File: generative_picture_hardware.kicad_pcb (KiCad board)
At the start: 2 copper layers, 100 x 100 mm, 63 parts, among them J1 e_Paper_HAT, J2 Conn_ARM_JTAG_SWD_10, J3 USB_C_Receptacle_USB2.0, Q1 PMN48XP, Q2 DMG9926UDM, Q3 MBT3904DW1, SW1 SW_Push, SW2 SW_Push, U1 AP2112K-3.3, U2 ESP32-WROOM-32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

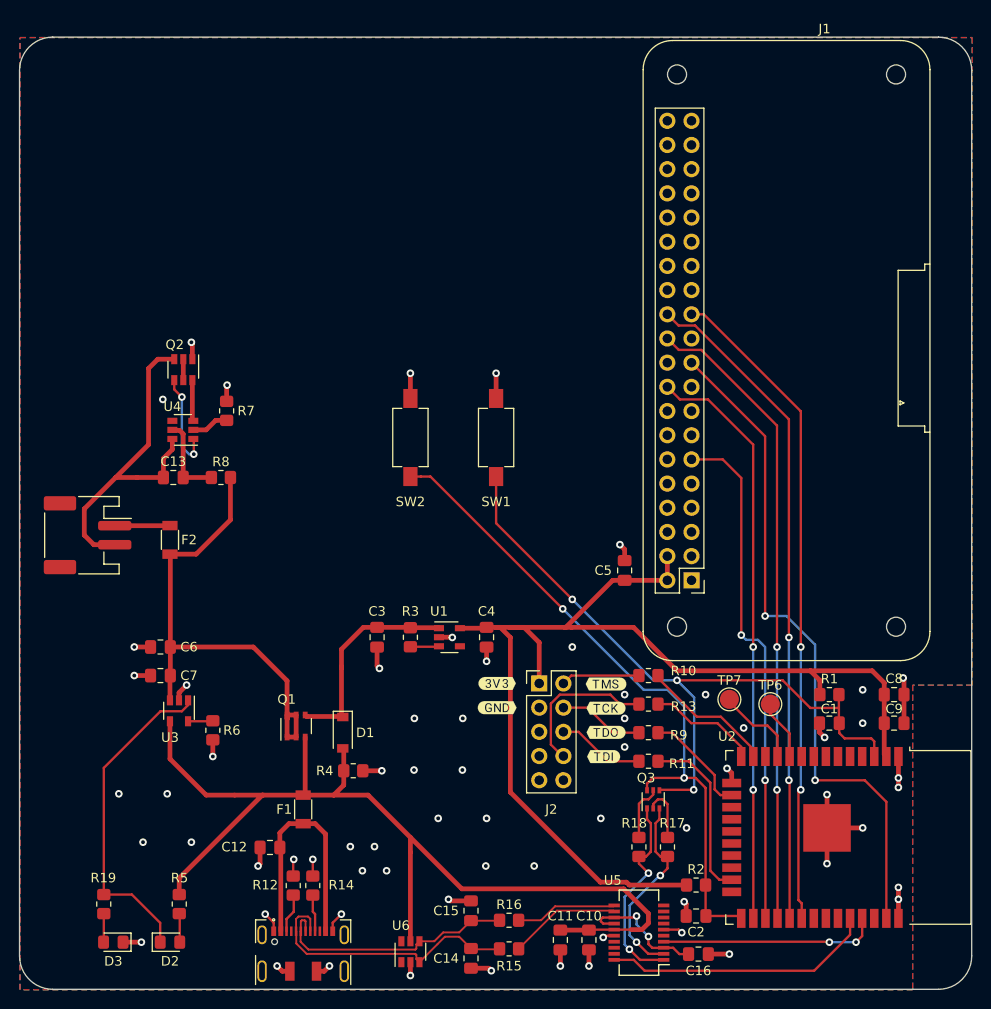
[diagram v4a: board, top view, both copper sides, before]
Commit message: Adds some more labels
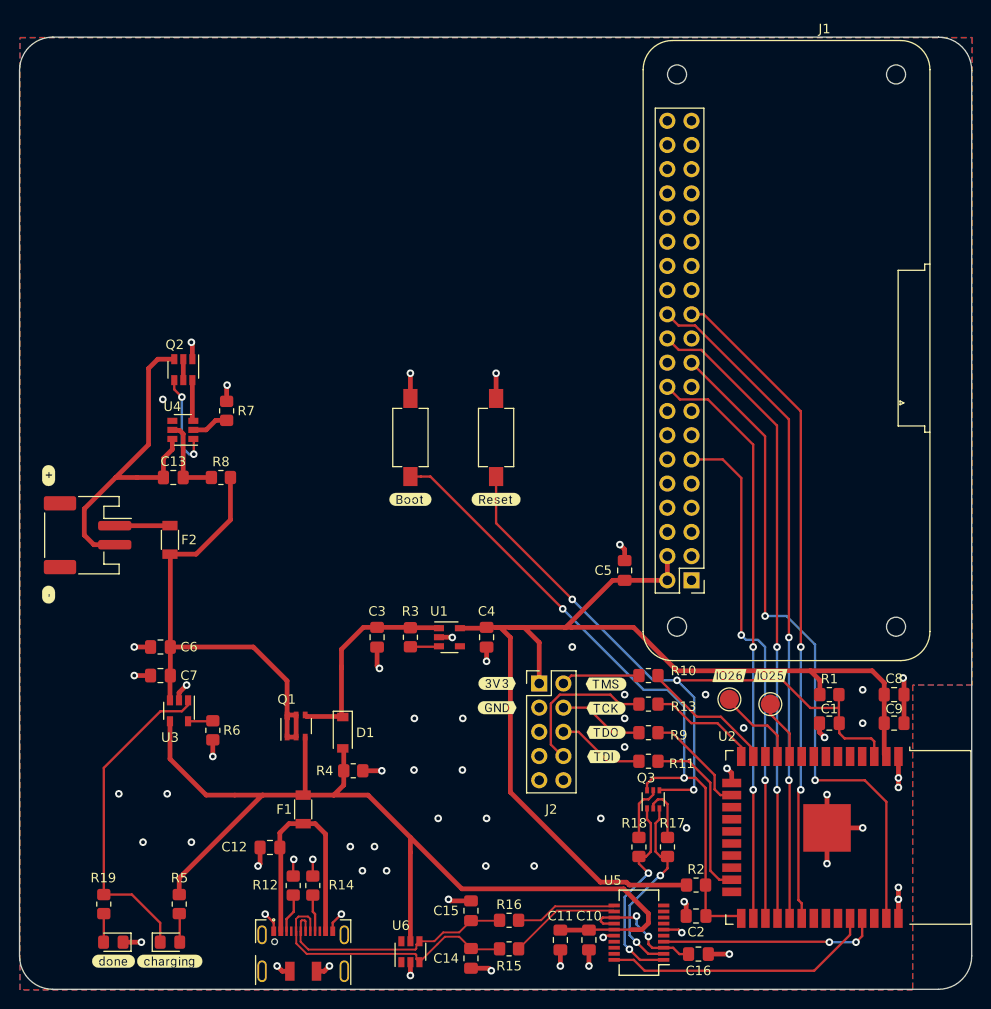
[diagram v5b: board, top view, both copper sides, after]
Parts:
- added ?: , buzzardLabel, F.Cu at (103.0, 110.5)
- added ?: , buzzardLabel, F.Cu at (141.0, 100.5)
- added ?: , buzzardLabel, F.Cu at (178.8, 119.0)
- added ?: , buzzardLabel, F.Cu at (103.0, 98.0)
- added ?: , buzzardLabel, F.Cu at (150.0, 100.5)
- added ?: , buzzardLabel, F.Cu at (115.7, 149.0)
- added ?: , buzzardLabel, F.Cu at (109.8, 149.0)
- added ?: , buzzardLabel, F.Cu at (174.5, 119.0)

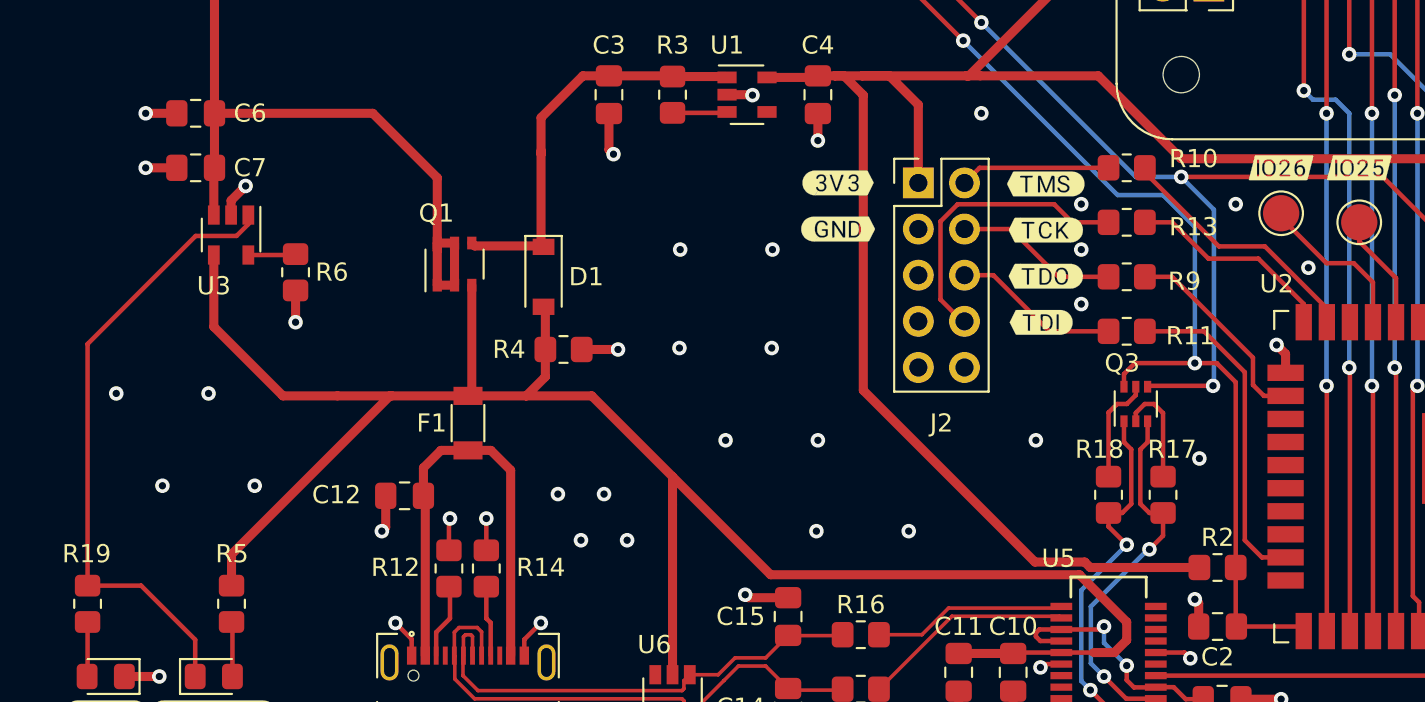
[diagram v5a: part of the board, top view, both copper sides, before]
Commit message: Cleans up the extra vias
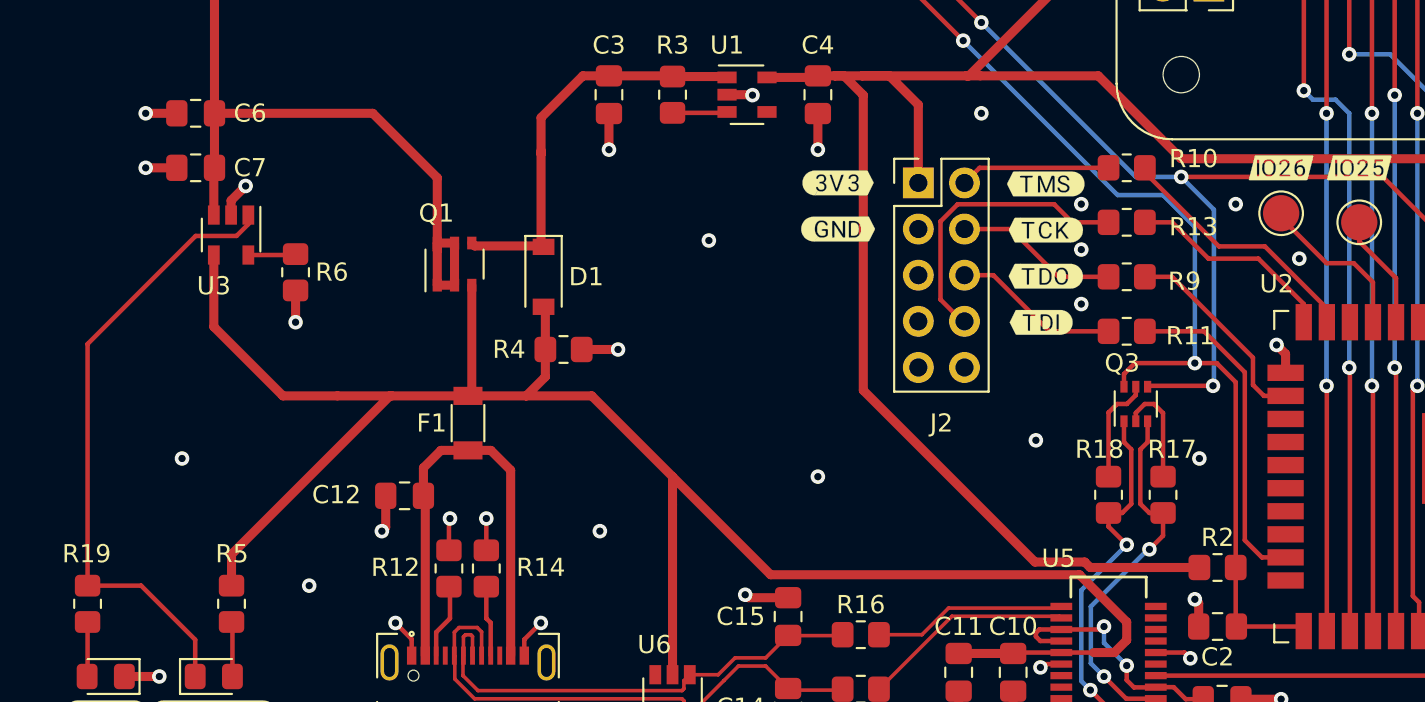
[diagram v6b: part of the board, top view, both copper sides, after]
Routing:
- net GND: track 82.3 -> 82.5 mm, vias 67 -> 56
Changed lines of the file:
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@@
   (segment (start 147.3625 149.7375) (end 149.2375 149.7375) (width 0.5) (layer "F.Cu") (net 3))
   (segment (start 169.9625 144.25) (end 169.9625 142.9625) (width 0.5) (layer "F.Cu") (net 3))
-  (segment (start 137.5 116.0125) (end 137.5 118) (width 0.5) (layer "F.Cu") (net 3))
   (segment (start 118.1 85.775) (end 118.1 84.1) (width 0.5) (layer "F.Cu") (net 3))
   (segment (start 147.3625 142.6625) (end 145.1625 142.6625) (width 0.5) (layer "F.Cu") (net 3))
@@
   (segment (start 136 129) (end 138 129) (width 0.5) (layer "F.Cu") (net 3))
   (segment (start 141 149.102479) (end 141 150.5) (width 0.5) (layer "F.Cu") (net 3))
-  (segment (start 137.5 118) (end 137.75 118.25) (width 0.5) (layer "F.Cu") (net 3))
+  (segment (start 149 116.0125) (end 149 118) (width 0.5) (layer "F.Cu") (net 3))
   (segment (start 192.75 119.25) (end 192.8375 119.3375) (width 0.5) (layer "F.Cu") (net 3))
   (segment (start 116.7 120.8) (end 117.5 120) (width 0.5) (layer "F.Cu") (net 3))
@@
   (segment (start 120.25 125.75) (end 120.25 127.5) (width 0.5) (layer "F.Cu") (net 3))
   (segment (start 161.4325 146.3175) (end 161.25 146.5) (width 0.25) (layer "F.Cu") (net 3))
+  (segment (start 137.5 118) (end 137.5 116.0125) (width 0.5) (layer "F.Cu") (net 3))
   (segment (start 128.6925 140.054098) (end 128.6925 138.361598) (width 0.25) (layer "F.Cu") (net 3))
   (segment (start 163.5 105.75) (end 163 105.25) (width 0.5) (layer "F.Cu") (net 3))
-  (segment (start 149 116.0125) (end 149 117.5) (width 0.5) (layer "F.Cu") (net 3))
   (segment (start 192.8375 119.3375) (end 192.8375 121) (width 0.5) (layer "F.Cu") (net 3))
   (segment (start 184.755 134.999748) (end 184.755 131.505) (width 0.5) (layer "F.Cu") (net 3))
@@
   (via (at 117.5 120) (size 0.8) (drill 0.4) (layers "F.Cu" "B.Cu") (net 3))
   (via (at 184.5 125.5) (size 0.8) (drill 0.4) (layers "F.Cu" "B.Cu") (net 3))
-  (via (at 146.46 128.92) (size 0.8) (drill 0.4) (layers "F.Cu" "B.Cu") (free) (net 3))
   (via (at 118 84) (size 0.8) (drill 0.4) (layers "F.Cu" "B.Cu") (net 3))
   (via (at 156.75 149.5) (size 0.8) (drill 0.4) (layers "F.Cu" "B.Cu") (net 3))
@@
   (via (at 120.25 127.5) (size 0.8) (drill 0.4) (layers "F.Cu" "B.Cu") (net 3))
   (via (at 163.5 126.5) (size 0.8) (drill 0.4) (layers "F.Cu" "B.Cu") (free) (net 3))
-  (via (at 137.23 136.96) (size 0.8) (drill 0.4) (layers "F.Cu" "B.Cu") (free) (net 3))
-  (via (at 176 124.5) (size 0.8) (drill 0.4) (layers "F.Cu" "B.Cu") (free) (net 3))
   (via (at 145.4 115) (size 0.8) (drill 0.4) (layers "F.Cu" "B.Cu") (net 3))
+  (via (at 137.5 118) (size 0.8) (drill 0.4) (layers "F.Cu" "B.Cu") (net 3))
   (via (at 130.75 138.304098) (size 0.8) (drill 0.4) (layers "F.Cu" "B.Cu") (net 3))
-  (via (at 110.38 131.42) (size 0.8) (drill 0.4) (layers "F.Cu" "B.Cu") (free) (net 3))
   (via (at 161 134) (size 0.8) (drill 0.4) (layers "F.Cu" "B.Cu") (free) (net 3))
   (via (at 128.75 138.304098) (size 0.8) (drill 0.4) (layers "F.Cu" "B.Cu") (net 3))
-  (via (at 143.92 134) (size 0.8) (drill 0.4) (layers "F.Cu" "B.Cu") (free) (net 3))
-  (via (at 148.92 139) (size 0.8) (drill 0.4) (layers "F.Cu" "B.Cu") (free) (net 3))
   (via (at 132.5 149.5) (size 0.8) (drill 0.4) (layers "F.Cu" "B.Cu") (net 3))
   (via (at 127 149.5) (size 0.8) (drill 0.4) (layers "F.Cu" "B.Cu") (net 3))
-  (via (at 112.92 136.5) (size 0.8) (drill 0.4) (layers "F.Cu" "B.Cu") (free) (net 3))
   (via (at 163.5 123.5) (size 0.8) (drill 0.4) (layers "F.Cu" "B.Cu") (free) (net 3))
   (via (at 133.75 144.054098) (size 0.8) (drill 0.4) (layers "F.Cu" "B.Cu") (net 3))
   (via (at 150 87.25) (size 0.8) (drill 0.4) (layers "F.Cu" "B.Cu") (net 3))
-  (via (at 149 134) (size 0.8) (drill 0.4) (layers "F.Cu" "B.Cu") (free) (net 3))
-  (via (at 149 117.5) (size 0.8) (drill 0.4) (layers "F.Cu" "B.Cu") (net 3))
-  (via (at 141.38 128.92) (size 0.8) (drill 0.4) (layers "F.Cu" "B.Cu") (free) (net 3))
-  (via (at 115.46 131.42) (size 0.8) (drill 0.4) (layers "F.Cu" "B.Cu") (free) (net 3))
-  (via (at 134.69 136.96) (size 0.8) (drill 0.4) (layers "F.Cu" "B.Cu") (free) (net 3))
   (via (at 192.75 119.25) (size 0.8) (drill 0.4) (layers "F.Cu" "B.Cu") (net 3))
   (via (at 141 87.25) (size 0.8) (drill 0.4) (layers "F.Cu" "B.Cu") (net 3))
   (via (at 121.75 88.5) (size 0.8) (drill 0.4) (layers "F.Cu" "B.Cu") (net 3))
+  (via (at 149 136) (size 0.8) (drill 0.4) (layers "F.Cu" "B.Cu") (free) (net 3))
   (via (at 184.75 131.5) (size 0.8) (drill 0.4) (layers "F.Cu" "B.Cu") (net 3))
-  (via (at 137.75 118.25) (size 0.8) (drill 0.4) (layers "F.Cu" "B.Cu") (net 3))
+  (via (at 149 118) (size 0.8) (drill 0.4) (layers "F.Cu" "B.Cu") (net 3))
+  (via (at 175.5 124) (size 0.8) (drill 0.4) (layers "F.Cu" "B.Cu") (free) (net 3))
   (via (at 141 150.5) (size 0.8) (drill 0.4) (layers "F.Cu" "B.Cu") (net 3))
   (via (at 158 116) (size 0.8) (drill 0.4) (layers "F.Cu" "B.Cu") (free) (net 3))
   (via (at 192.25 130.75) (size 0.8) (drill 0.4) (layers "F.Cu" "B.Cu") (net 3))
   (via (at 170 135) (size 0.8) (drill 0.4) (layers "F.Cu" "B.Cu") (free) (net 3))
-  (via (at 118 136.5) (size 0.8) (drill 0.4) (layers "F.Cu" "B.Cu") (free) (net 3))
   (via (at 149.5 150) (size 0.8) (drill 0.4) (layers "F.Cu" "B.Cu") (net 3))
   (via (at 172 121) (size 0.8) (drill 0.4) (layers "F.Cu" "B.Cu") (free) (net 3))
   (via (at 159.75 149.5) (size 0.8) (drill 0.4) (layers "F.Cu" "B.Cu") (net 3))
   (via (at 112.75 147) (size 0.8) (drill 0.4) (layers "F.Cu" "B.Cu") (net 3))
-  (via (at 135.96 139.5) (size 0.8) (drill 0.4) (layers "F.Cu" "B.Cu") (free) (net 3))
-  (via (at 146.5 123.5) (size 0.8) (drill 0.4) (layers "F.Cu" "B.Cu") (free) (net 3))
   (via (at 138 129) (size 0.8) (drill 0.4) (layers "F.Cu" "B.Cu") (net 3))
+  (via (at 114 135) (size 0.8) (drill 0.4) (layers "F.Cu" "B.Cu") (free) (net 3))
   (via (at 145 142.5) (size 0.8) (drill 0.4) (layers "F.Cu" "B.Cu") (net 3))
   (via (at 169.5 146) (size 0.8) (drill 0.4) (layers "F.Cu" "B.Cu") (net 3))
@@
   (via (at 192.25 142.5) (size 0.8) (drill 0.4) (layers "F.Cu" "B.Cu") (net 3))
   (via (at 125 139) (size 0.8) (drill 0.4) (layers "F.Cu" "B.Cu") (net 3))
-  (via (at 138.5 139.5) (size 0.8) (drill 0.4) (layers "F.Cu" "B.Cu") (free) (net 3))
+  (via (at 137 139) (size 0.8) (drill 0.4) (layers "F.Cu" "B.Cu") (free) (net 3))
+  (via (at 143 123) (size 0.8) (drill 0.4) (layers "F.Cu" "B.Cu") (free) (net 3))
   (via (at 174.25 128.75) (size 0.8) (drill 0.4) (layers "F.Cu" "B.Cu") (net 3))
-  (via (at 141.42 123.5) (size 0.8) (drill 0.4) (layers "F.Cu" "B.Cu") (free) (net 3))
+  (via (at 121 142) (size 0.8) (drill 0.4) (layers "F.Cu" "B.Cu") (free) (net 3))
   (via (at 192.25 141.25) (size 0.8) (drill 0.4) (layers "F.Cu" "B.Cu") (net 3))
   (via (at 188.5 135) (size 0.8) (drill 0.4) (layers "F.Cu" "B.Cu") (net 3))
@@
   (via (at 161.25 146.5) (size 0.8) (drill 0.4) (layers "F.Cu" "B.Cu") (net 3))
   (via (at 174.5 148.25) (size 0.8) (drill 0.4) (layers "F.Cu" "B.Cu") (net 3))
-  (via (at 154 139) (size 0.8) (drill 0.4) (layers "F.Cu" "B.Cu") (free) (net 3))
   (segment (start 186 122.4) (end 186 123.9625) (width 0.25) (layer "F.Cu") (net 4))
   (segment (start 167.2 131) (end 167.15 131.05) (width 0.25) (layer "F.Cu") (net 4))

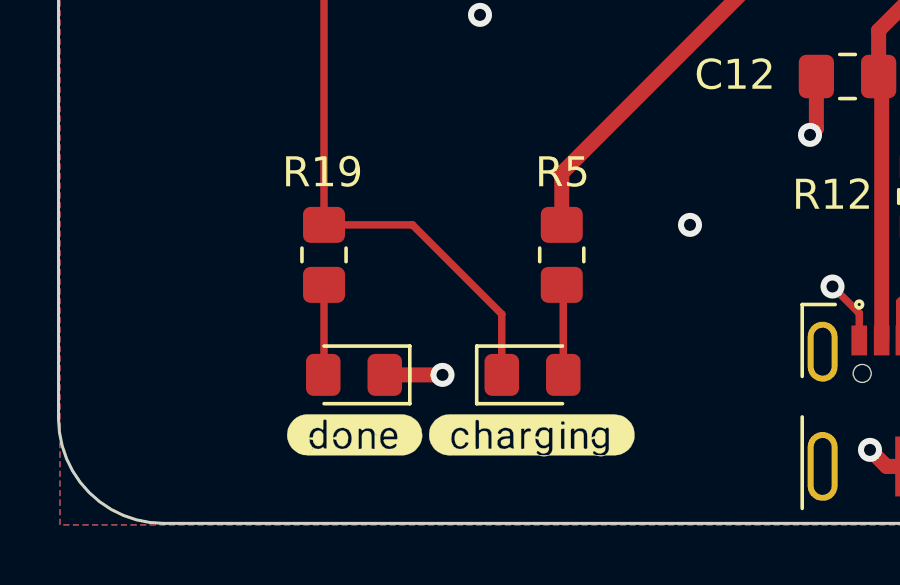
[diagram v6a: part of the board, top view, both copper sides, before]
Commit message: Adds logo
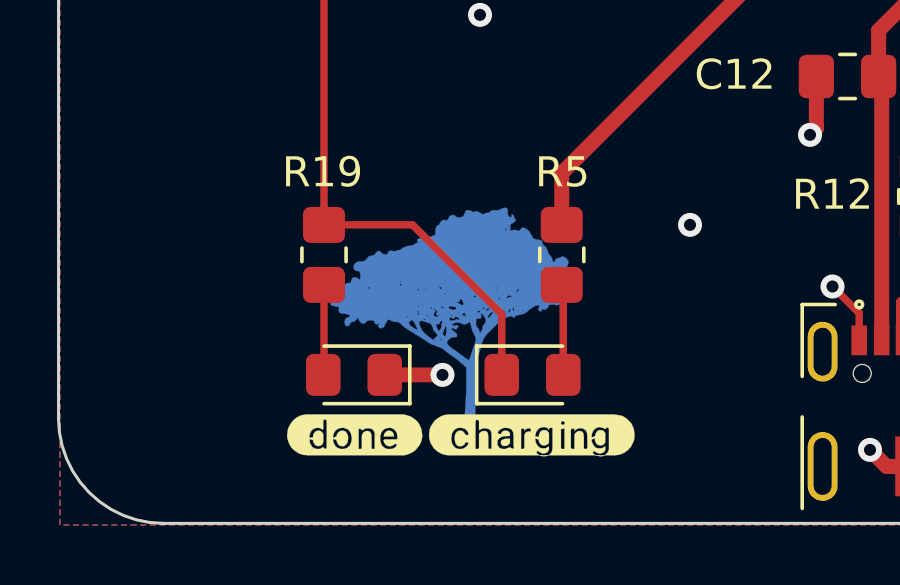
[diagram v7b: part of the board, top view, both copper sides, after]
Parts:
- added Ref**: Val**, Amieiro:url_bsilks, F.Cu at (113.0, 150.0)
- added Ref**: Val**, Amieiro:ipe_logo, F.Cu at (113.0, 145.0)
